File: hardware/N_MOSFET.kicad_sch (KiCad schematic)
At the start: 4 parts, among them Q2 Q_NMOS_GSD

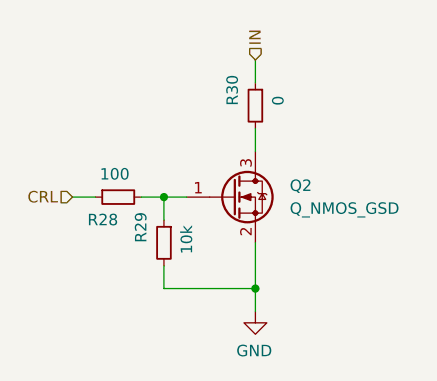
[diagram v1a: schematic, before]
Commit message: debuged the board, changed one opto for mosfet, changed the way water and potentiometers were supplied. Also standrised opamps (yoinked opamps from data Data_Acquisition_Cards)
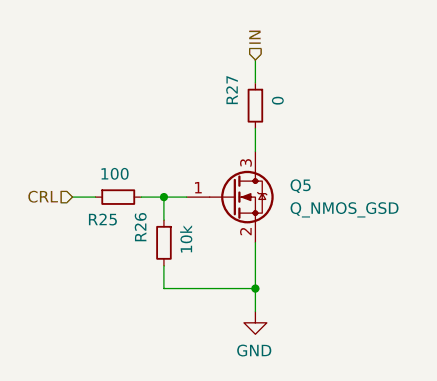
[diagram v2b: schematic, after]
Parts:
- renumbered Q2 to Q5, R28 to R25, R29 to R26, R30 to R27
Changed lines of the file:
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@@
   (symbol (lib_id "Device:R_Small") (at 153.67 107.95 0) (mirror y)
     (in_bom yes) (on_board yes)
-    (property "Reference" "R29" (id 0) (at 151.13 107.95 90)
+    (property "Reference" "R26" (id 0) (at 151.13 107.95 90)
       (effects (font (size 1.27 1.27)) (justify left))
     )
@@
   (symbol (lib_id "Device:R_Small") (at 148.59 102.87 90) (mirror x)
     (in_bom yes) (on_board yes)
-    (property "Reference" "R28" (id 0) (at 148.59 105.41 90)
+    (property "Reference" "R25" (id 0) (at 148.59 105.41 90)
       (effects (font (size 1.27 1.27)) (justify left))
     )
@@
   (symbol (lib_id "Device:R_Small") (at 163.83 92.71 0) (mirror y)
     (in_bom yes) (on_board yes)
-    (property "Reference" "R30" (id 0) (at 161.29 92.71 90)
+    (property "Reference" "R27" (id 0) (at 161.29 92.71 90)
       (effects (font (size 1.27 1.27)) (justify left))
     )
@@
   (symbol (lib_id "Device:Q_NMOS_GSD") (at 161.29 102.87 0)
     (in_bom yes) (on_board yes) (fields_autoplaced)
-    (property "Reference" "Q2" (id 0) (at 167.64 101.5999 0)
+    (property "Reference" "Q5" (id 0) (at 167.64 101.5999 0)
       (effects (font (size 1.27 1.27)) (justify left))
     )

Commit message: nameing scheme update
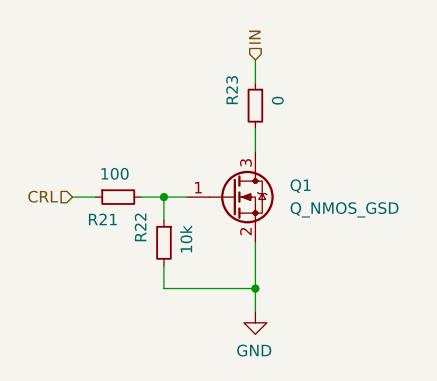
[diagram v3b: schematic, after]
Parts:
- renumbered Q5 to Q1, R25 to R21, R26 to R22, R27 to R23
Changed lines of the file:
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@@
   (symbol (lib_id "Device:R_Small") (at 153.67 107.95 0) (mirror y)
     (in_bom yes) (on_board yes)
-    (property "Reference" "R26" (id 0) (at 151.13 107.95 90)
+    (property "Reference" "R22" (id 0) (at 151.13 107.95 90)
       (effects (font (size 1.27 1.27)) (justify left))
     )
@@
   (symbol (lib_id "Device:R_Small") (at 148.59 102.87 90) (mirror x)
     (in_bom yes) (on_board yes)
-    (property "Reference" "R25" (id 0) (at 148.59 105.41 90)
+    (property "Reference" "R21" (id 0) (at 148.59 105.41 90)
       (effects (font (size 1.27 1.27)) (justify left))
     )
@@
   (symbol (lib_id "Device:R_Small") (at 163.83 92.71 0) (mirror y)
     (in_bom yes) (on_board yes)
-    (property "Reference" "R27" (id 0) (at 161.29 92.71 90)
+    (property "Reference" "R23" (id 0) (at 161.29 92.71 90)
       (effects (font (size 1.27 1.27)) (justify left))
     )
@@
   (symbol (lib_id "power:GND") (at 163.83 115.57 0) (mirror y)
     (in_bom yes) (on_board yes)
-    (property "Reference" "#PWR0107" (id 0) (at 163.83 121.92 0)
+    (property "Reference" "#PWR0106" (id 0) (at 163.83 121.92 0)
       (effects (font (size 1.27 1.27)) hide)
     )
@@
   (symbol (lib_id "Device:Q_NMOS_GSD") (at 161.29 102.87 0)
     (in_bom yes) (on_board yes) (fields_autoplaced)
-    (property "Reference" "Q5" (id 0) (at 167.64 101.5999 0)
+    (property "Reference" "Q1" (id 0) (at 167.64 101.5999 0)
       (effects (font (size 1.27 1.27)) (justify left))
     )
